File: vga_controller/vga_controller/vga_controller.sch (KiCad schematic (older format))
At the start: 7 parts, among them U1 74LS161, U2 74LS161, U3 74LS161, U4 74LS161, U5 74LS161, U6 74LS161, X1 ACO-xxxMHz-A

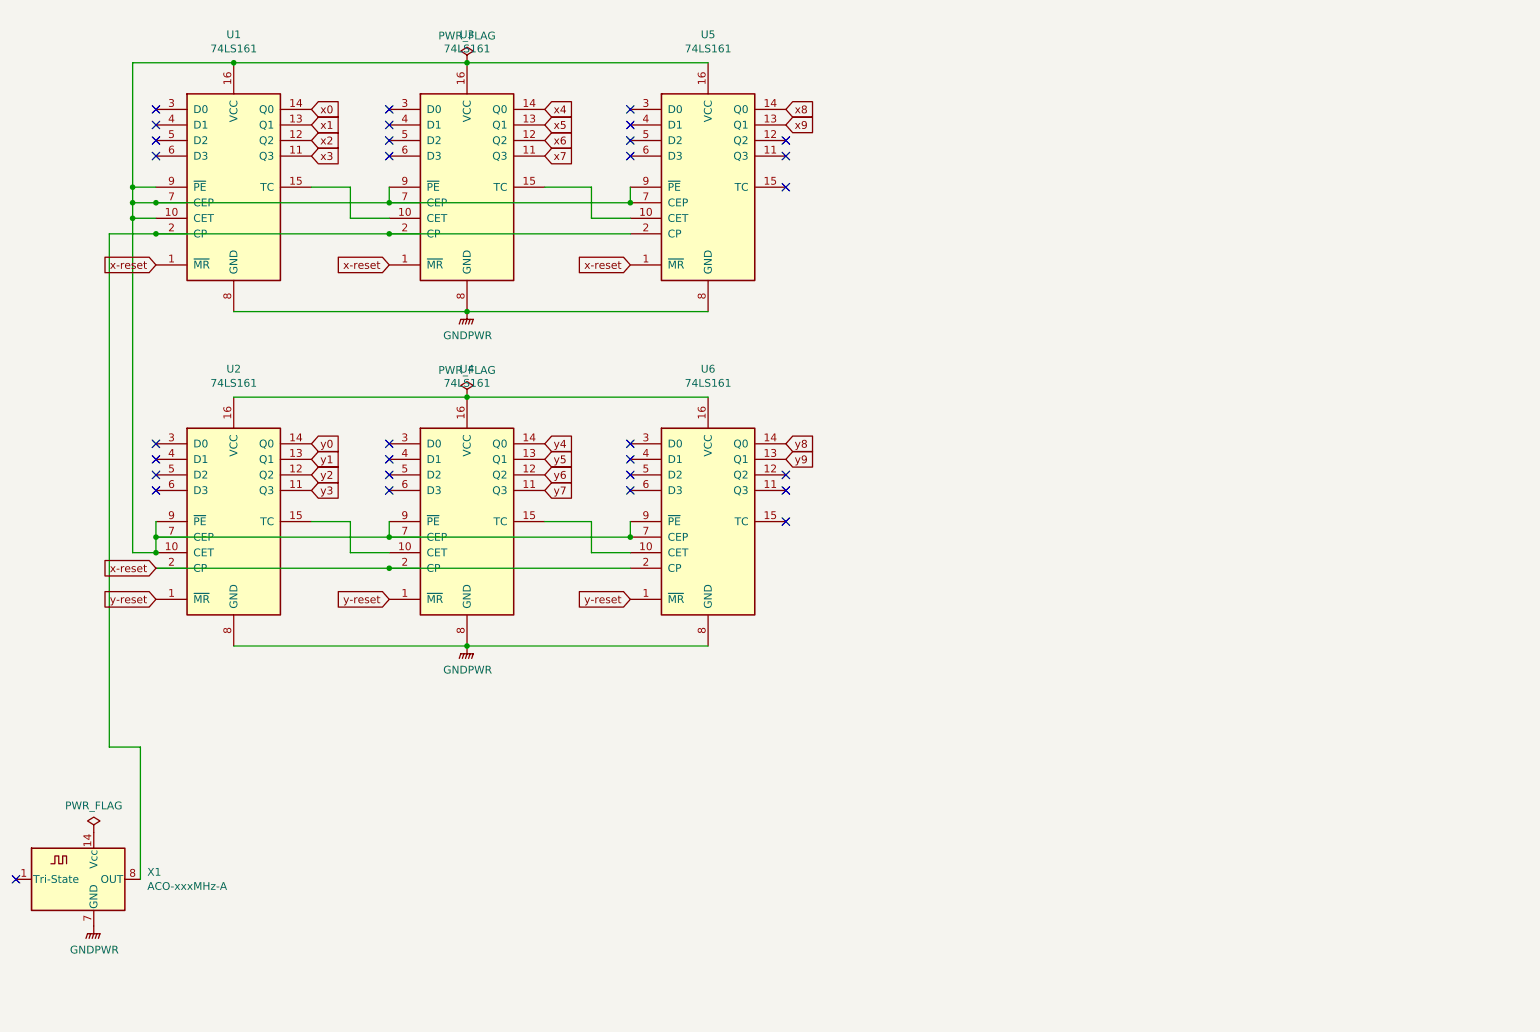
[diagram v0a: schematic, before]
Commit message: added sub-sheets
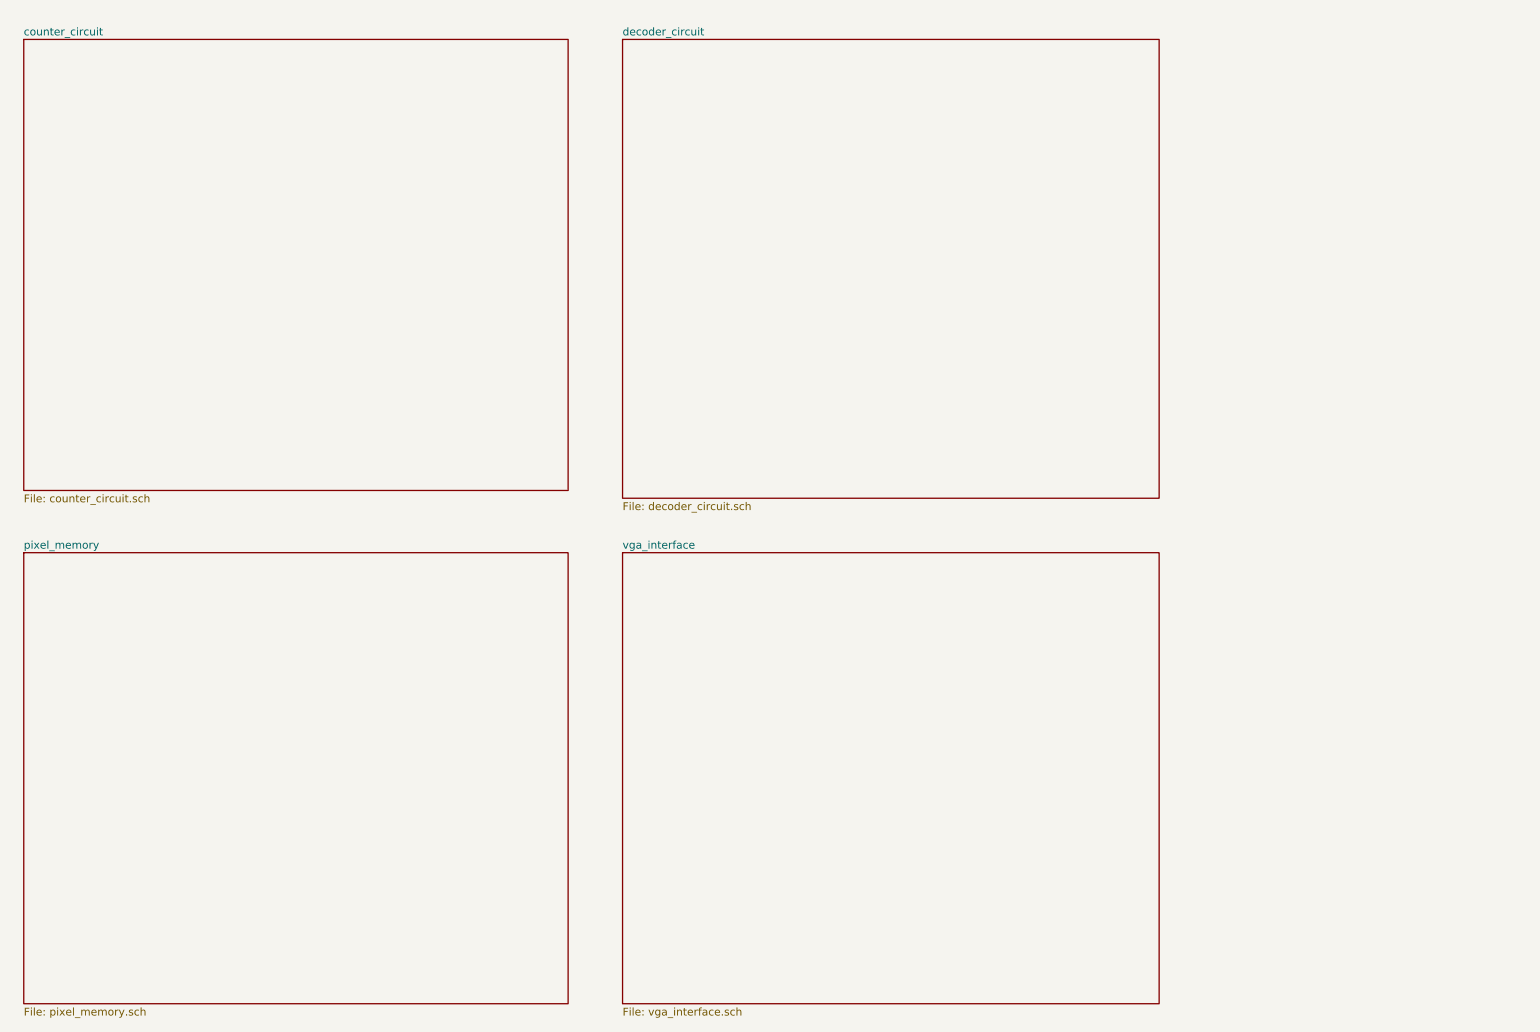
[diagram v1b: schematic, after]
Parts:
- removed U1, U2, U3, U4, U5, U6: 74LS161, symbol 74xx:74LS161
- removed X1: ACO-xxxMHz-A, Oscillator:Oscillator_DIP-14, symbol Oscillator:ACO-xxxMHz-A
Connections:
- no-connect marks 31 -> 0

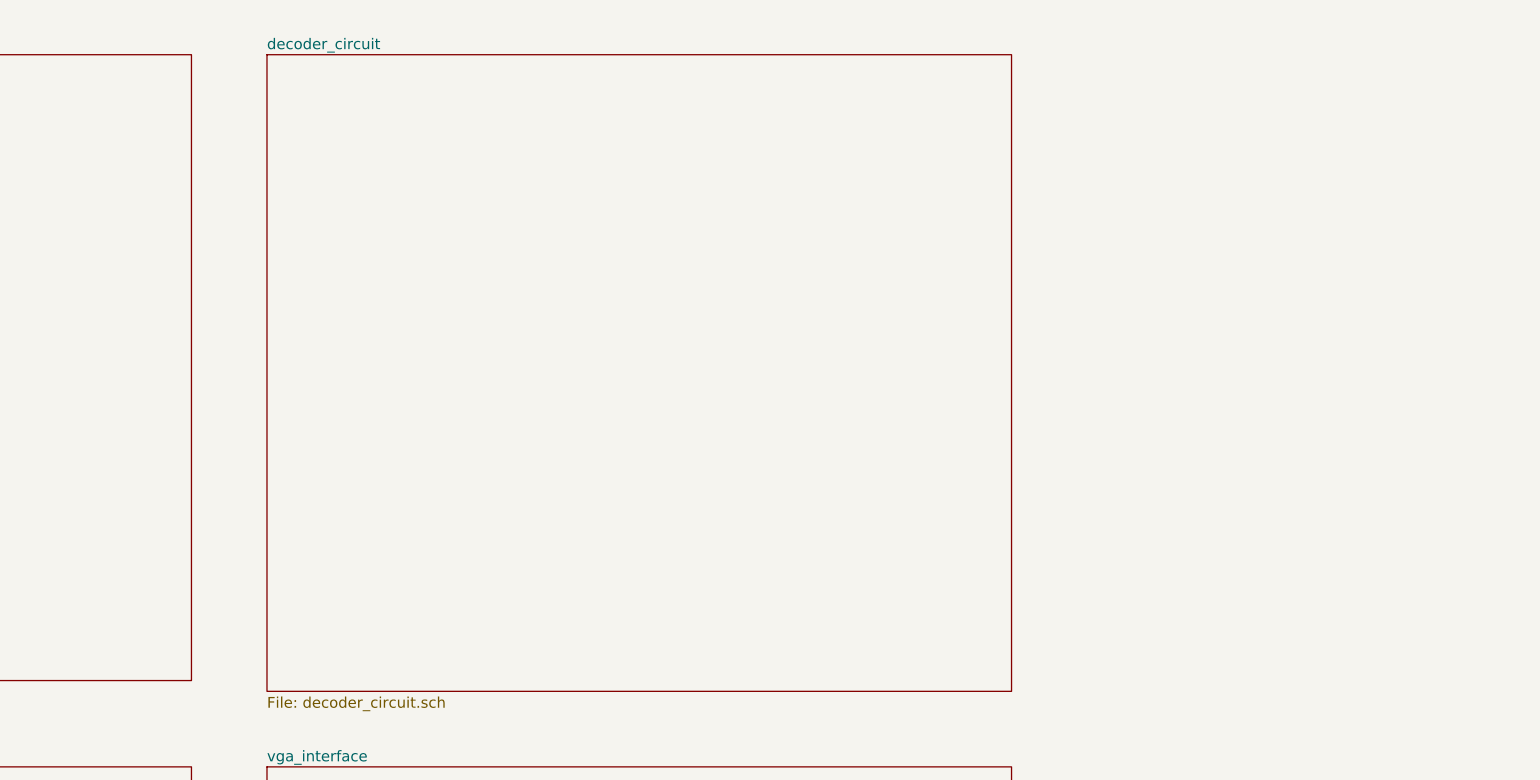
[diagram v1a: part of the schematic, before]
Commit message: added correct labels, supressed errors
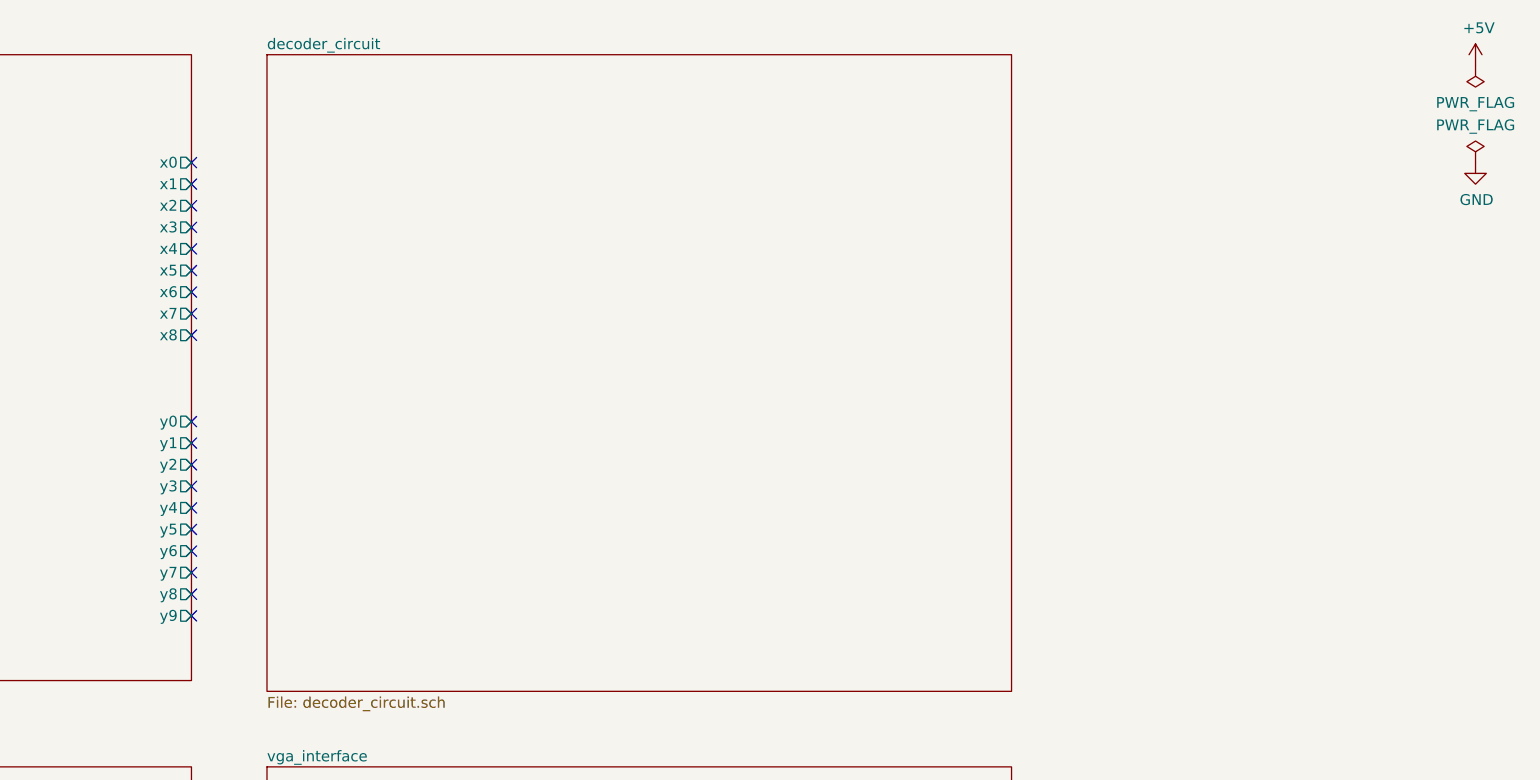
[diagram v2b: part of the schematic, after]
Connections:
- no-connect marks 0 -> 19
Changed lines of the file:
@@
 $EndDescr
-$Sheet
-S 800  700  3500 2900
-U 5E7A10F5
-F0 "counter_circuit" 50
-F1 "counter_circuit.sch" 50
-$EndSheet
 $Sheet
 S 4650 700  3450 2950
@@
 F1 "vga_interface.sch" 50
 $EndSheet
+$Sheet
+S 800  700  3500 2900
+U 5E7A10F5
+F0 "counter_circuit" 50
+F1 "counter_circuit.sch" 50
+F2 "y9" O R 4300 3300 50
+F3 "y8" O R 4300 3200 50
+F4 "y7" O R 4300 3100 50
+F5 "y6" O R 4300 3000 50
+F6 "y5" O R 4300 2900 50
+F7 "y4" O R 4300 2800 50
+F8 "y3" O R 4300 2700 50
+F9 "y2" O R 4300 2600 50
+F10 "y1" O R 4300 2500 50
+F11 "y0" O R 4300 2400 50
+F12 "x8" O R 4300 2000 50
+F13 "x7" O R 4300 1900 50
+F14 "x6" O R 4300 1800 50
+F15 "x5" O R 4300 1700 50
+F16 "x4" O R 4300 1600 50
+F17 "x3" O R 4300 1500 50
+F18 "x2" O R 4300 1400 50
+F19 "x1" O R 4300 1300 50
+F20 "x0" O R 4300 1200 50
+$EndSheet
+NoConn ~ 4300 1200
+NoConn ~ 4300 1300
+NoConn ~ 4300 1400
+NoConn ~ 4300 1500
+NoConn ~ 4300 1600
+NoConn ~ 4300 1700
+NoConn ~ 4300 1800
+NoConn ~ 4300 1900
+NoConn ~ 4300 2000
+NoConn ~ 4300 2400
+NoConn ~ 4300 2500
+NoConn ~ 4300 2600
+NoConn ~ 4300 2700
+NoConn ~ 4300 2800
+NoConn ~ 4300 2900
+NoConn ~ 4300 3000
+NoConn ~ 4300 3100
+NoConn ~ 4300 3200
+NoConn ~ 4300 3300
+$Comp
+L power:+5V #PWR0105
+U 1 1 5E772D7F
+P 10250 750
+F 0 "#PWR0105" H 10250 600 50  0001 C CNN
+F 1 "+5V" H 10265 923 50  0000 C CNN
+F 2 "" H 10250 750 50  0001 C CNN
+F 3 "" H 10250 750 50  0001 C CNN
+	1    10250 750
+	1    0    0    -1
+$EndComp
+$Comp
+L power:GND #PWR0106
+U 1 1 5E77329E
+P 10250 1200
+F 0 "#PWR0106" H 10250 950 50  0001 C CNN
+F 1 "GND" H 10255 1027 50  0000 C CNN
+F 2 "" H 10250 1200 50  0001 C CNN
+F 3 "" H 10250 1200 50  0001 C CNN
+	1    10250 1200
+	1    0    0    -1
+$EndComp
+$Comp
+L power:PWR_FLAG #FLG0101
+U 1 1 5E77346B
+P 10250 750
+F 0 "#FLG0101" H 10250 825 50  0001 C CNN
+F 1 "PWR_FLAG" H 10250 923 50  0000 C CNN
+F 2 "" H 10250 750 50  0001 C CNN
+F 3 "~" H 10250 750 50  0001 C CNN
+	1    10250 750
+	-1   0    0    1
+$EndComp
+$Comp
+L power:PWR_FLAG #FLG0102
+U 1 1 5E773925
+P 10250 1200
+F 0 "#FLG0102" H 10250 1275 50  0001 C CNN
+F 1 "PWR_FLAG" H 10250 1373 50  0000 C CNN
+F 2 "" H 10250 1200 50  0001 C CNN
+F 3 "~" H 10250 1200 50  0001 C CNN
+	1    10250 1200
+	1    0    0    -1
+$EndComp
 $EndSCHEMATC

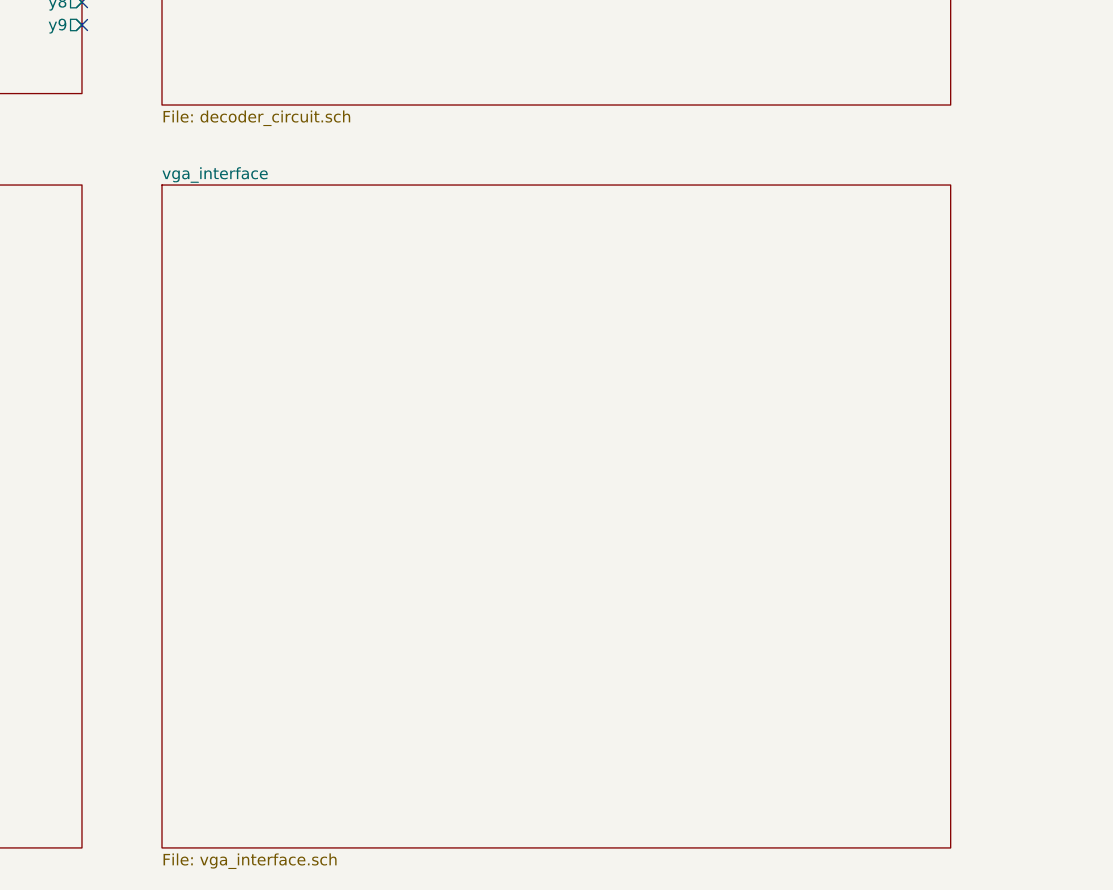
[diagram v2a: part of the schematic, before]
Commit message: removed interface sheet, combined with pixel_memory
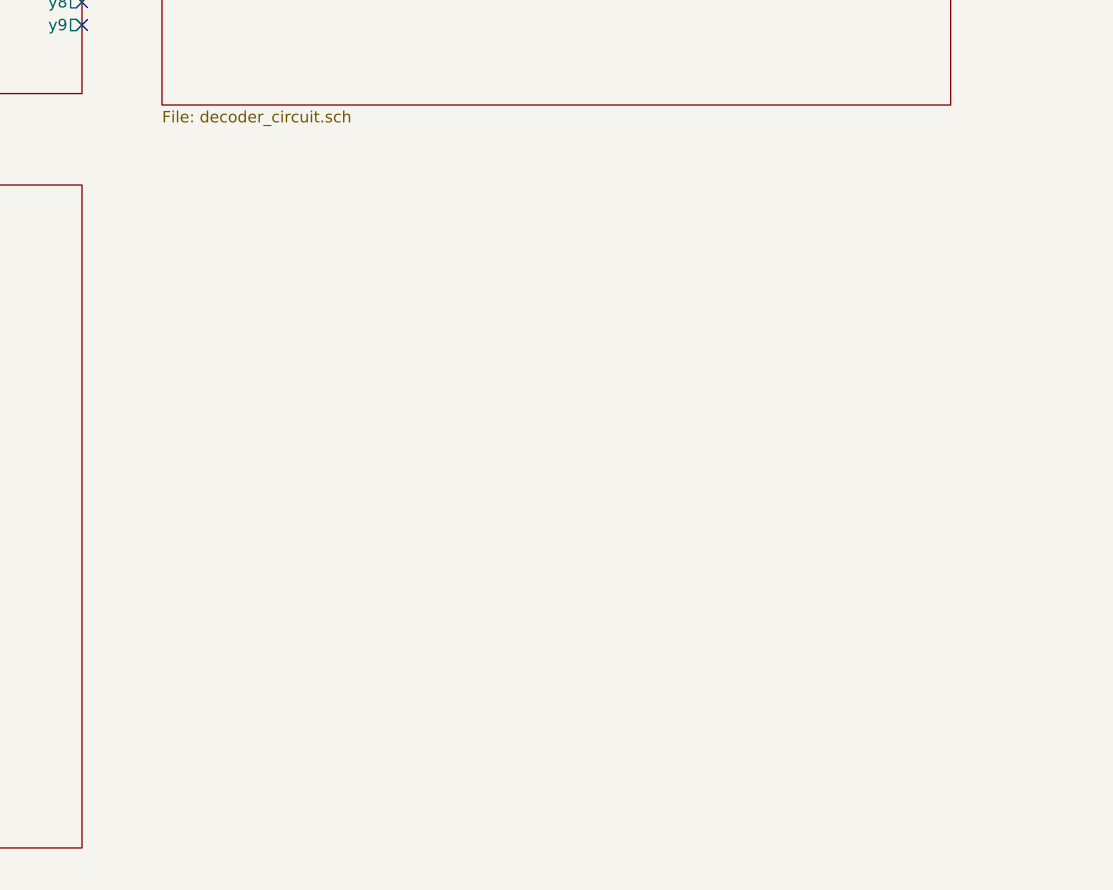
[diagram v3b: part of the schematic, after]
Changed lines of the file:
@@
 $Descr A4 11693 8268
 encoding utf-8
-Sheet 1 5
+Sheet 1 4
 Title ""
 Date ""
@@
 $EndSheet
 $Sheet
-S 4650 4000 3450 2900
-U 5E7FD01A
-F0 "vga_interface" 50
-F1 "vga_interface.sch" 50
-$EndSheet
-$Sheet

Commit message: made interconnects
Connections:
- no-connect marks 19 -> 0
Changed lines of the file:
@@
 F0 "decoder_circuit" 50
 F1 "decoder_circuit.sch" 50
+F2 "x0" I L 4650 1200 50
+F3 "x1" I L 4650 1300 50
+F4 "x2" I L 4650 1400 50
+F5 "x3" I L 4650 1500 50
+F6 "x4" I L 4650 1600 50
+F7 "x5" I L 4650 1700 50
+F8 "x6" I L 4650 1800 50
+F9 "x7" I L 4650 1900 50
+F10 "x8" I L 4650 2000 50
+F11 "y0" I L 4650 2400 50
+F12 "y1" I L 4650 2500 50
+F13 "y2" I L 4650 2600 50
+F14 "y3" I L 4650 2700 50
+F15 "y4" I L 4650 2800 50
+F16 "y5" I L 4650 2900 50
+F17 "y6" I L 4650 3000 50
+F18 "y7" I L 4650 3100 50
+F19 "y8" I L 4650 3200 50
+F20 "y9" I L 4650 3300 50
 $EndSheet
 $Sheet
@@
 F1 "pixel_memory.sch" 50
 $EndSheet
+$Comp
+L power:+5V #PWR01
+U 1 1 5E772D7F
+P 10250 750
+F 0 "#PWR01" H 10250 600 50  0001 C CNN
+F 1 "+5V" H 10265 923 50  0000 C CNN
+F 2 "" H 10250 750 50  0001 C CNN
+F 3 "" H 10250 750 50  0001 C CNN
+	1    10250 750
+	1    0    0    -1
+$EndComp
+$Comp
+L power:GND #PWR02
+U 1 1 5E77329E
+P 10250 1200
+F 0 "#PWR02" H 10250 950 50  0001 C CNN
+F 1 "GND" H 10255 1027 50  0000 C CNN
+F 2 "" H 10250 1200 50  0001 C CNN
+F 3 "" H 10250 1200 50  0001 C CNN
+	1    10250 1200
+	1    0    0    -1
+$EndComp
+$Comp
+L power:PWR_FLAG #FLG01
+U 1 1 5E77346B
+P 10250 750
+F 0 "#FLG01" H 10250 825 50  0001 C CNN
+F 1 "PWR_FLAG" H 10250 923 50  0000 C CNN
+F 2 "" H 10250 750 50  0001 C CNN
+F 3 "~" H 10250 750 50  0001 C CNN
+	1    10250 750
+	-1   0    0    1
+$EndComp
+$Comp
+L power:PWR_FLAG #FLG02
+U 1 1 5E773925
+P 10250 1200
+F 0 "#FLG02" H 10250 1275 50  0001 C CNN
+F 1 "PWR_FLAG" H 10250 1373 50  0000 C CNN
+F 2 "" H 10250 1200 50  0001 C CNN
+F 3 "~" H 10250 1200 50  0001 C CNN
+	1    10250 1200
+	1    0    0    -1
+$EndComp
+Wire Wire Line
+	4300 1200 4650 1200
+Wire Wire Line
+	4300 1300 4650 1300
+Wire Wire Line
+	4300 1400 4650 1400
+Wire Wire Line
+	4300 1500 4650 1500
+Wire Wire Line
+	4300 1600 4650 1600
+Wire Wire Line
+	4300 1700 4650 1700
+Wire Wire Line
+	4300 1800 4650 1800
+Wire Wire Line
+	4300 1900 4650 1900
+Wire Wire Line
+	4300 2000 4650 2000
 $Sheet
 S 800  700  3500 2900
@@
 F20 "x0" O R 4300 1200 50
 $EndSheet
-NoConn ~ 4300 1200
-NoConn ~ 4300 1300
-NoConn ~ 4300 1400
-NoConn ~ 4300 1500
-NoConn ~ 4300 1600
-NoConn ~ 4300 1700
-NoConn ~ 4300 1800
-NoConn ~ 4300 1900
-NoConn ~ 4300 2000
-NoConn ~ 4300 2400
-NoConn ~ 4300 2500
-NoConn ~ 4300 2600
-NoConn ~ 4300 2700
-NoConn ~ 4300 2800
-NoConn ~ 4300 2900
-NoConn ~ 4300 3000
-NoConn ~ 4300 3100
-NoConn ~ 4300 3200
-NoConn ~ 4300 3300
-$Comp
-L power:+5V #PWR0105
-U 1 1 5E772D7F
-P 10250 750
-F 0 "#PWR0105" H 10250 600 50  0001 C CNN
-F 1 "+5V" H 10265 923 50  0000 C CNN
-F 2 "" H 10250 750 50  0001 C CNN
-F 3 "" H 10250 750 50  0001 C CNN
-	1    10250 750
-	1    0    0    -1
-$EndComp
-$Comp
-L power:GND #PWR0106
-U 1 1 5E77329E
-P 10250 1200
-F 0 "#PWR0106" H 10250 950 50  0001 C CNN
-F 1 "GND" H 10255 1027 50  0000 C CNN
-F 2 "" H 10250 1200 50  0001 C CNN
-F 3 "" H 10250 1200 50  0001 C CNN
-	1    10250 1200
-	1    0    0    -1
-$EndComp
-$Comp
-L power:PWR_FLAG #FLG0101
-U 1 1 5E77346B
-P 10250 750
-F 0 "#FLG0101" H 10250 825 50  0001 C CNN
-F 1 "PWR_FLAG" H 10250 923 50  0000 C CNN
-F 2 "" H 10250 750 50  0001 C CNN
-F 3 "~" H 10250 750 50  0001 C CNN
-	1    10250 750
-	-1   0    0    1
-$EndComp
-$Comp
-L power:PWR_FLAG #FLG0102
-U 1 1 5E773925
-P 10250 1200
-F 0 "#FLG0102" H 10250 1275 50  0001 C CNN
-F 1 "PWR_FLAG" H 10250 1373 50  0000 C CNN
-F 2 "" H 10250 1200 50  0001 C CNN
-F 3 "~" H 10250 1200 50  0001 C CNN
-	1    10250 1200
-	1    0    0    -1
-$EndComp
+Wire Wire Line
+	4300 2400 4650 2400
+Wire Wire Line
+	4300 2500 4650 2500
+Wire Wire Line
+	4300 2600 4650 2600
+Wire Wire Line
+	4300 2700 4650 2700
+Wire Wire Line
+	4300 2800 4650 2800
+Wire Wire Line
+	4300 2900 4650 2900
+Wire Wire Line
+	4300 3000 4650 3000
+Wire Wire Line
+	4300 3100 4650 3100
+Wire Wire Line
+	4300 3200 4650 3200
+Wire Wire Line
+	4300 3300 4650 3300
 $EndSCHEMATC
